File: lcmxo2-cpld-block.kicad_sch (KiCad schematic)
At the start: 42 parts, among them J1005 JTAG JUMP, J12 PMOD, J13 Raspberry_Pi_2_3, J6001 Conn_02x06_Odd_Even, SW6 BTN, SW7 BTN, SW8 BTN, U9 LCMXO2-1200HC-4TG100I

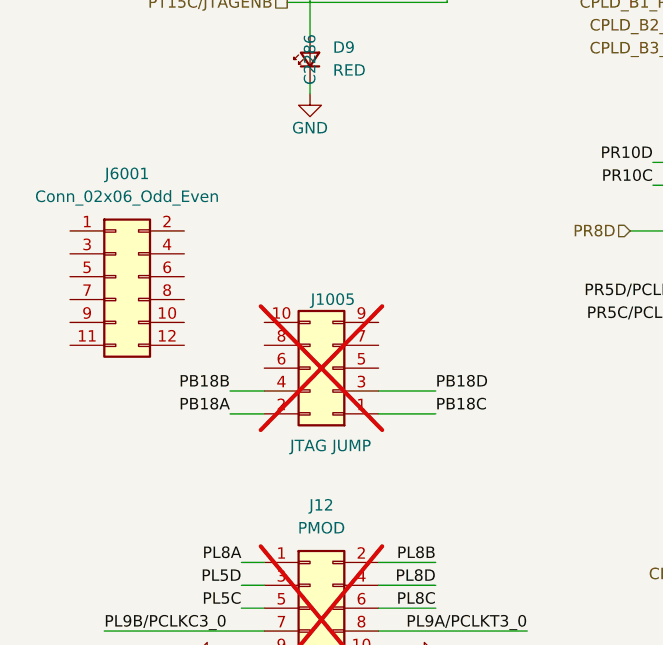
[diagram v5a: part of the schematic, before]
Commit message: Improve the routing
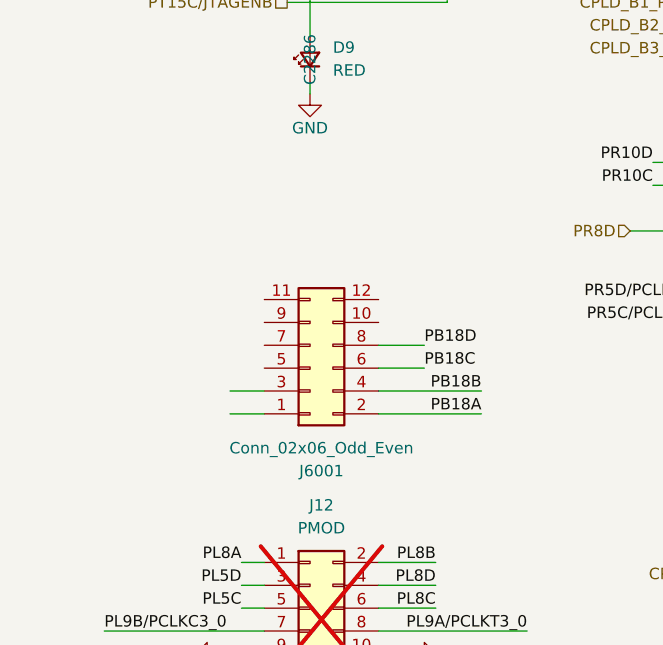
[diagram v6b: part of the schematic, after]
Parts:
- removed J1005: JTAG JUMP, Connector_PinSocket_2.54mm:PinSocket_2x05_P2.54mm_Vertical, symbol Connector_Generic:Conn_02x05_Odd_Even
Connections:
- net PB18A: now also J6001.2 (Pin_2)
- net PB18B: now also J6001.4 (Pin_4)
- net PB18C: now also J6001.6 (Pin_6)
- net PB18D: now also J6001.8 (Pin_8)
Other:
- moved on the sheet: J6001
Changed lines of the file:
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@@
 	(wire
 		(pts
+			(xy 49.53 143.51) (xy 44.45 143.51)
+		)
+		(stroke
+			(width 0)
+			(type default)
+		)
+	)
+	(wire
+		(pts
 			(xy 227.33 25.4) (xy 227.33 26.67)
 		)
@@
 	(wire
 		(pts
+			(xy 49.53 140.97) (xy 44.45 140.97)
+		)
+		(stroke
+			(width 0)
+			(type default)
+		)
+	)
+	(wire
+		(pts
 			(xy 261.62 36.83) (xy 252.73 36.83)
 		)
@@
 	(wire
 		(pts
-			(xy 50.8 146.05) (xy 44.45 146.05)
+			(xy 55.88 146.05) (xy 44.45 146.05)
 		)
 		(stroke
@@
 	(wire
 		(pts
-			(xy 50.8 148.59) (xy 44.45 148.59)
+			(xy 55.88 148.59) (xy 44.45 148.59)
 		)
 		(stroke
@@
 	)
 	(label "PB18A"
-		(at 27.94 148.59 180)
+		(at 55.88 148.59 180)
 		(effects
 			(font
@@
 	)
 	(label "PB18D"
-		(at 50.8 146.05 0)
+		(at 49.53 140.97 0)
 		(effects
 			(font
@@
 	)
 	(label "PB18B"
-		(at 27.94 146.05 180)
+		(at 55.88 146.05 180)
 		(effects
 			(font
@@
 	)
 	(label "PB18C"
-		(at 50.8 148.59 0)
+		(at 49.53 143.51 0)
 		(effects
 			(font
@@
 	)
 	(symbol
-		(lib_id "Connector_Generic:Conn_02x05_Odd_Even")
-		(at 39.37 143.51 180)
-		(unit 1)
-		(exclude_from_sim no)
-		(in_bom no)
-		(on_board yes)
-		(dnp yes)
-		(property "Reference" "J1005"
-			(at 39.37 135.89 0)
-			(effects
-				(font
-					(size 1.27 1.27)
-				)
-			)
-		)
-		(property "Value" "JTAG JUMP"
-			(at 39.116 152.146 0)
-			(effects
-				(font
-					(size 1.27 1.27)
-				)
-			)
-		)
-		(property "Footprint" "Connector_PinSocket_2.54mm:PinSocket_2x05_P2.54mm_Vertical"
-			(at 39.37 120.142 0)
-			(effects
-				(font
-					(size 1.27 1.27)
-				)
-				(hide yes)
-			)
-		)
-		(property "Datasheet" "~"
-			(at 39.37 143.51 0)
-			(effects
-				(font
-					(size 1.27 1.27)
-				)
-				(hide yes)
-			)
-		)
-		(property "Description" "Generic connector, double row, 02x05, odd/even pin numbering scheme (row 1 odd numbers, row 2 even numbers), script generated (kicad-library-utils/schlib/autogen/connector/)"
-			(at 39.37 143.51 0)
-			(effects
-				(font
-					(size 1.27 1.27)
-				)
-				(hide yes)
-			)
-		)
-		(pin "6"
-		)
-		(pin "3"
-		)
-		(pin "10"
-		)
-		(pin "4"
-		)
-		(pin "7"
-		)
-		(pin "1"
-		)
-		(pin "9"
-		)
-		(pin "8"
-		)
-		(pin "5"
-		)
-		(pin "2"
-		)
-		(instances
-			(project "stm32-fpga-bootloader"
-				(path "/5ed49623-6cbc-4a61-8fb3-1814d185ddb6/78f79e27-5991-443e-9657-8ff8f155d4b1"
-					(reference "J1005")
-					(unit 1)
-				)
-			)
-		)
-	)
-	(symbol
 		(lib_id "Device:C_Small")
 		(at 167.64 33.02 0)
@@
 	(symbol
 		(lib_id "Connector_Generic:Conn_02x06_Odd_Even")
-		(at 15.24 133.35 0)
+		(at 36.83 143.51 0)
+		(mirror x)
 		(unit 1)
 		(exclude_from_sim no)
@@
 		(on_board yes)
 		(dnp no)
-		(fields_autoplaced yes)
 		(property "Reference" "J6001"
-			(at 16.51 121.92 0)
+			(at 38.1 154.94 0)
 			(effects
 				(font
@@
 		)
 		(property "Value" "Conn_02x06_Odd_Even"
-			(at 16.51 124.46 0)
+			(at 38.1 152.4 0)
 			(effects
 				(font
@@
 		)
 		(property "Footprint" "Connector_PinSocket_2.54mm:PinSocket_2x06_P2.54mm_Vertical"
-			(at 15.24 133.35 0)
+			(at 36.83 143.51 0)
 			(effects
 				(font
@@
 		)
 		(property "Datasheet" "~"
-			(at 15.24 133.35 0)
+			(at 36.83 143.51 0)
 			(effects
 				(font
@@
 		)
 		(property "Description" "Generic connector, double row, 02x06, odd/even pin numbering scheme (row 1 odd numbers, row 2 even numbers), script generated (kicad-library-utils/schlib/autogen/connector/)"
-			(at 15.24 133.35 0)
+			(at 36.83 143.51 0)
 			(effects
 				(font

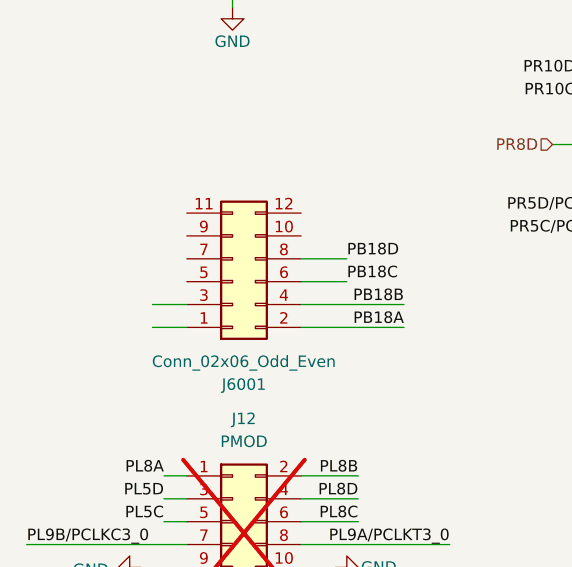
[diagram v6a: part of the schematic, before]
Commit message: Improve the routing
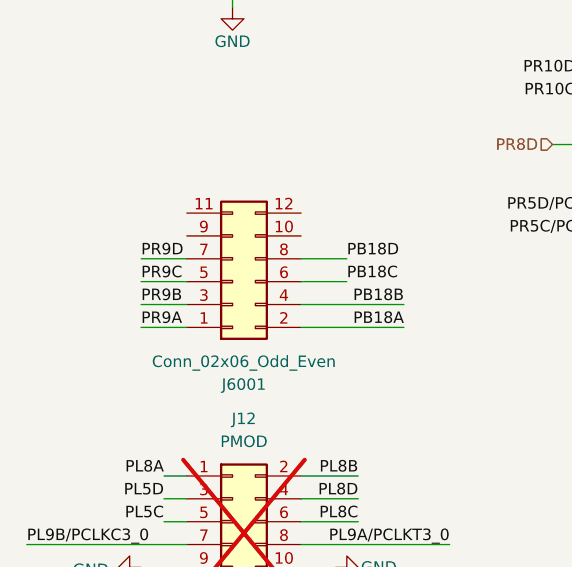
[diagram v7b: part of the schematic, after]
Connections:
- net PR9A: now also J6001.1 (Pin_1)
- net PR9B: now also J6001.3 (Pin_3)
- net PR9C: now also J6001.5 (Pin_5)
- net PR9D: now also J6001.7 (Pin_7)
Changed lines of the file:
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@@
 	(wire
 		(pts
-			(xy 27.94 146.05) (xy 31.75 146.05)
+			(xy 26.67 146.05) (xy 31.75 146.05)
 		)
 		(stroke
@@
 	(wire
 		(pts
-			(xy 27.94 148.59) (xy 31.75 148.59)
+			(xy 26.67 148.59) (xy 31.75 148.59)
 		)
 		(stroke
@@
 	(wire
 		(pts
+			(xy 26.67 143.51) (xy 31.75 143.51)
+		)
+		(stroke
+			(width 0)
+			(type default)
+		)
+	)
+	(wire
+		(pts
 			(xy 205.74 67.31) (xy 212.09 67.31)
 		)
@@
 		(pts
 			(xy 163.83 151.13) (xy 157.48 151.13)
+		)
+		(stroke
+			(width 0)
+			(type default)
+		)
+	)
+	(wire
+		(pts
+			(xy 26.67 140.97) (xy 31.75 140.97)
 		)
 		(stroke
@@
 		)
 	)
+	(label "PR9D"
+		(at 26.67 140.97 0)
+		(effects
+			(font
+				(size 1.27 1.27)
+			)
+			(justify left bottom)
+		)
+	)
 	(label "PR5D/PCLKC1_0"
 		(at 81.28 135.89 180)
@@
 		)
 	)
+	(label "PR9C"
+		(at 26.67 143.51 0)
+		(effects
+			(font
+				(size 1.27 1.27)
+			)
+			(justify left bottom)
+		)
+	)
 	(label "PB18A"
 		(at 55.88 148.59 180)
@@
 		)
 	)
+	(label "PR9B"
+		(at 26.67 146.05 0)
+		(effects
+			(font
+				(size 1.27 1.27)
+			)
+			(justify left bottom)
+		)
+	)
 	(label "PB4D"
 		(at 261.62 36.83 180)
@@
 		(effects
 			(font
+				(size 1.27 1.27)
+			)
+			(justify left bottom)
+		)
+	)
+	(label "PR9A"
+		(at 26.67 148.59 0)
+		(effects
+			(font
